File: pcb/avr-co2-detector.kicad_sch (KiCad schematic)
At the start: 16 parts

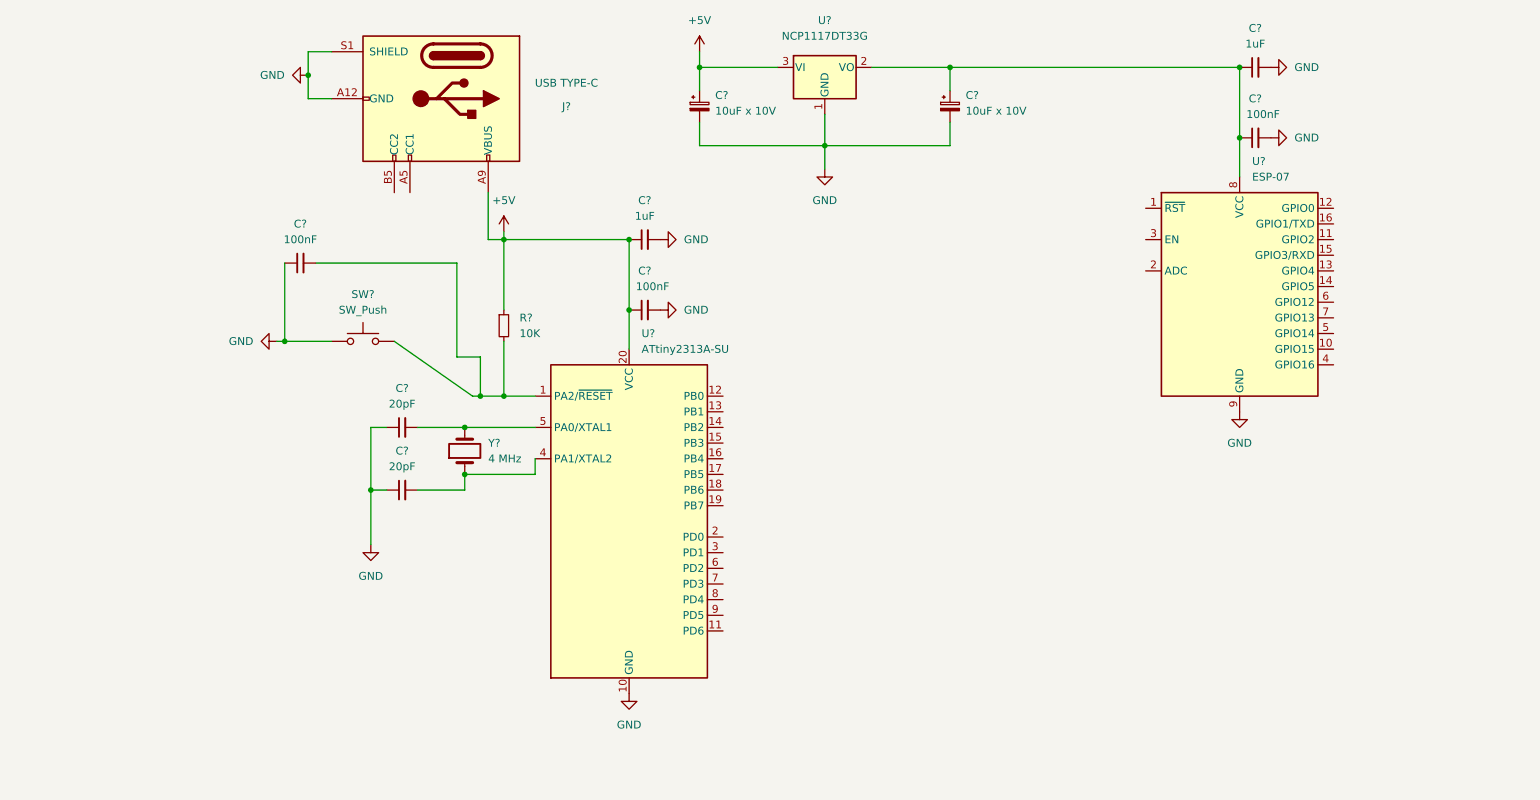
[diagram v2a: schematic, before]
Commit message: Added reset circuit and connector for programming ESP-07
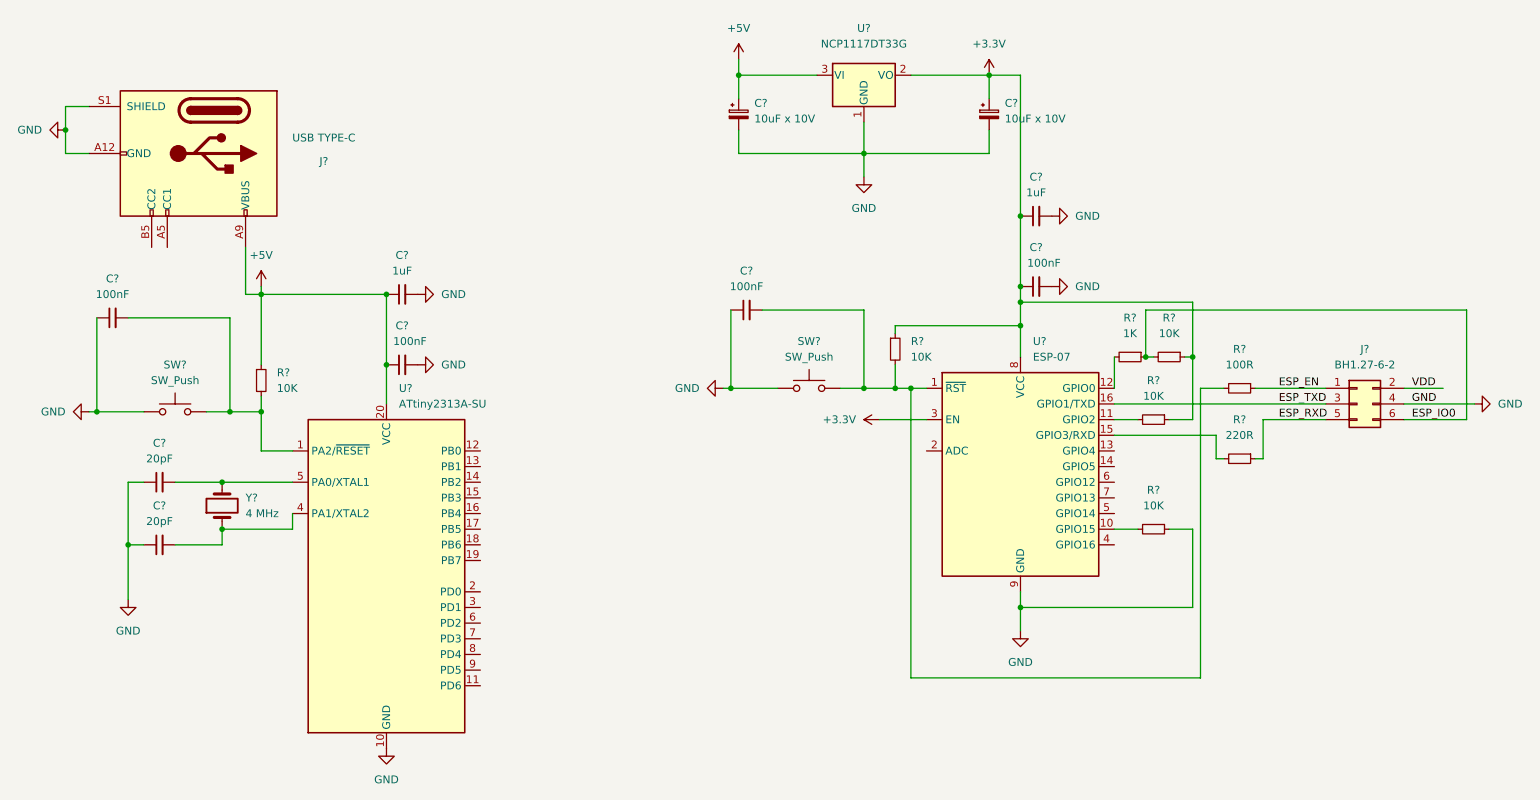
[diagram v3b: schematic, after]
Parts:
- added C?: 100nF, symbol Device:C_Small
- added J?: BH1.27-6-2, symbol Connector_Generic:Conn_02x03_Odd_Even
- added R?: 220R, symbol Device:R_Small
- added R?: 100R, symbol Device:R_Small
- added R? (x4): 10K, symbol Device:R_Small
- added R?: 1K, symbol Device:R_Small
- added SW?: SW_Push, symbol Switch:SW_Push
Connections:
- net GND: now also C?.1, J?.4 (Pin_4), R?.1, SW?.1
- net at U?.1 (~{RST}): now also C?.2, R?.2, R?.2, SW?.2
- net at U?.10 (GPIO15): now also R?.2
- net at U?.11 (GPIO2): now also R?.2
- net at U?.12 (GPIO0): now also R?.2
- net at U?.15 (GPIO3/RXD): now also R?.2
- net ESP_TXD: now reaches U?.16 (GPIO1/TXD)
- net ESP_TXD: now also J?.3 (Pin_3)
- net +3.3V: now reaches U?.3 (EN)
- net +3.3V: now also C?.1, C?.1, C?.1, U?.2 (VO), U?.8 (VCC), R?.1, R?.1, R?.1
- new net ESP_EN: J?.1 (Pin_1), R?.1
- new net ESP_IO0: J?.6 (Pin_6), R?.1, R?.2
- new net ESP_RXD: J?.5 (Pin_5), R?.1
- new net VDD: J?.2 (Pin_2)
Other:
- moved on the sheet: C?, J?, R?, SW?, U?, Y?

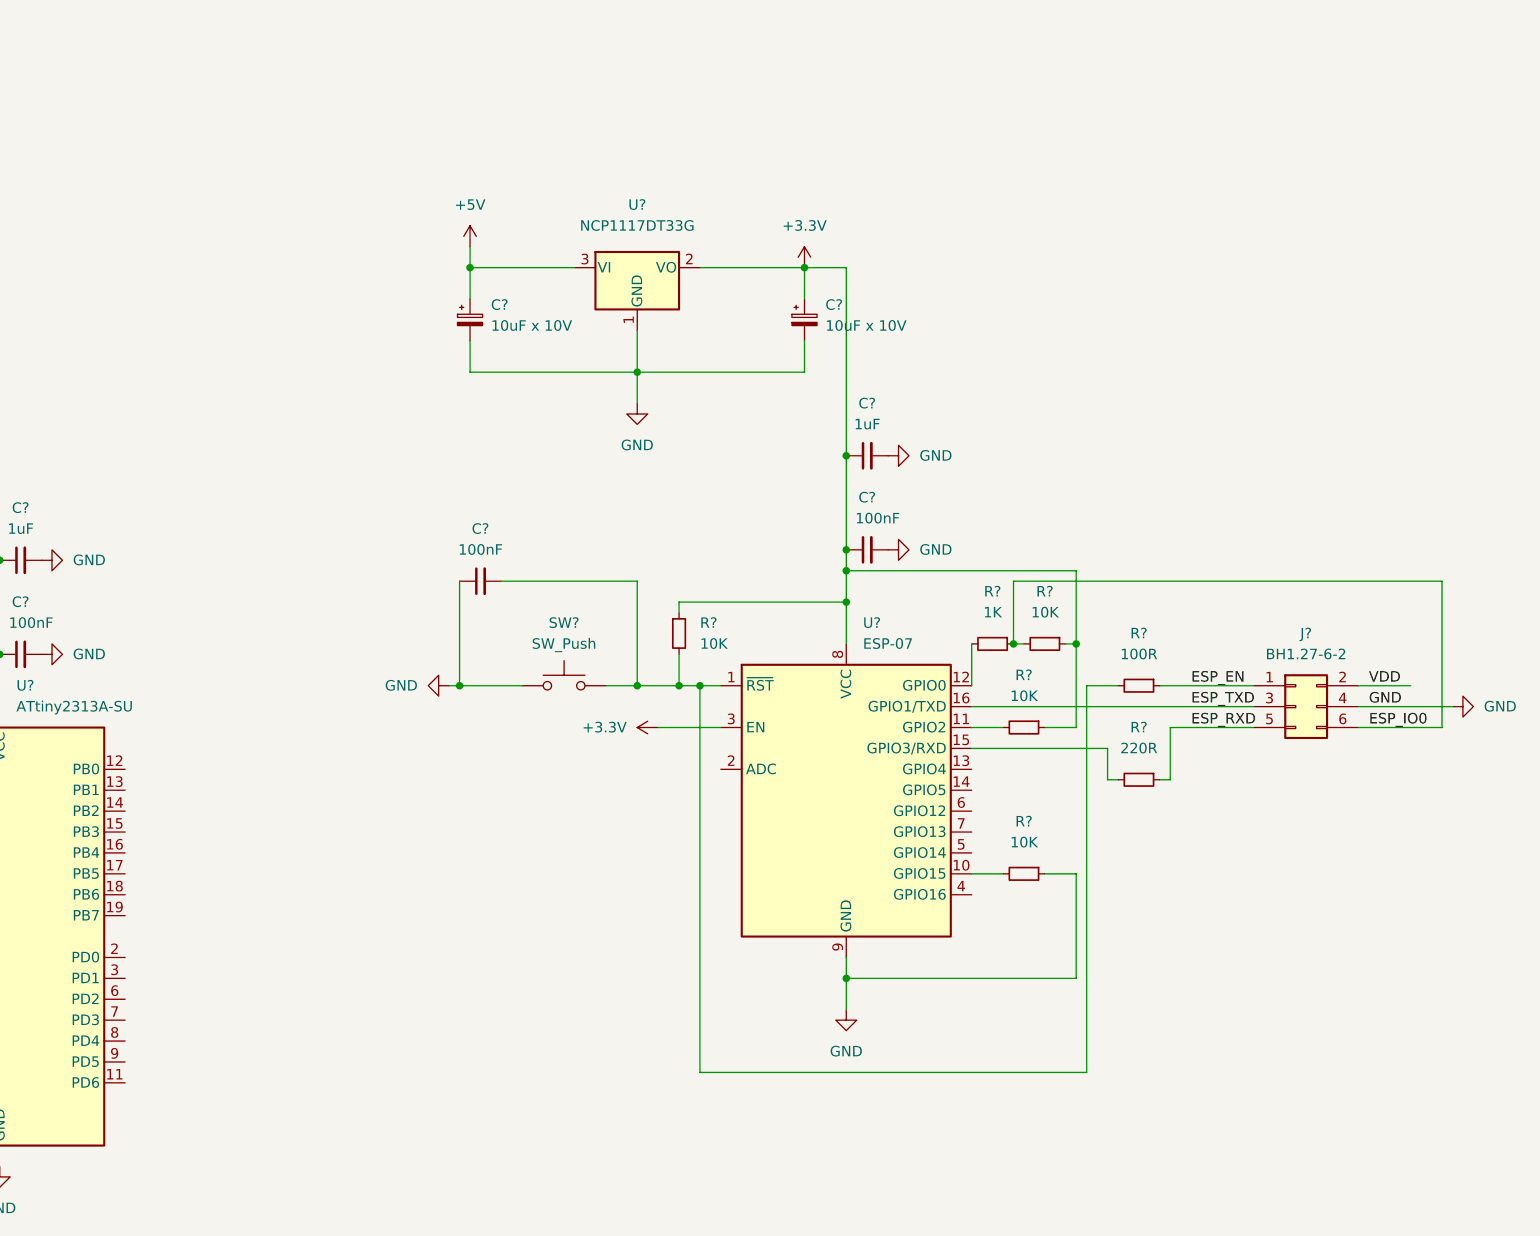
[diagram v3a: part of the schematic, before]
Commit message: Added level shifters for ESP-07 UART
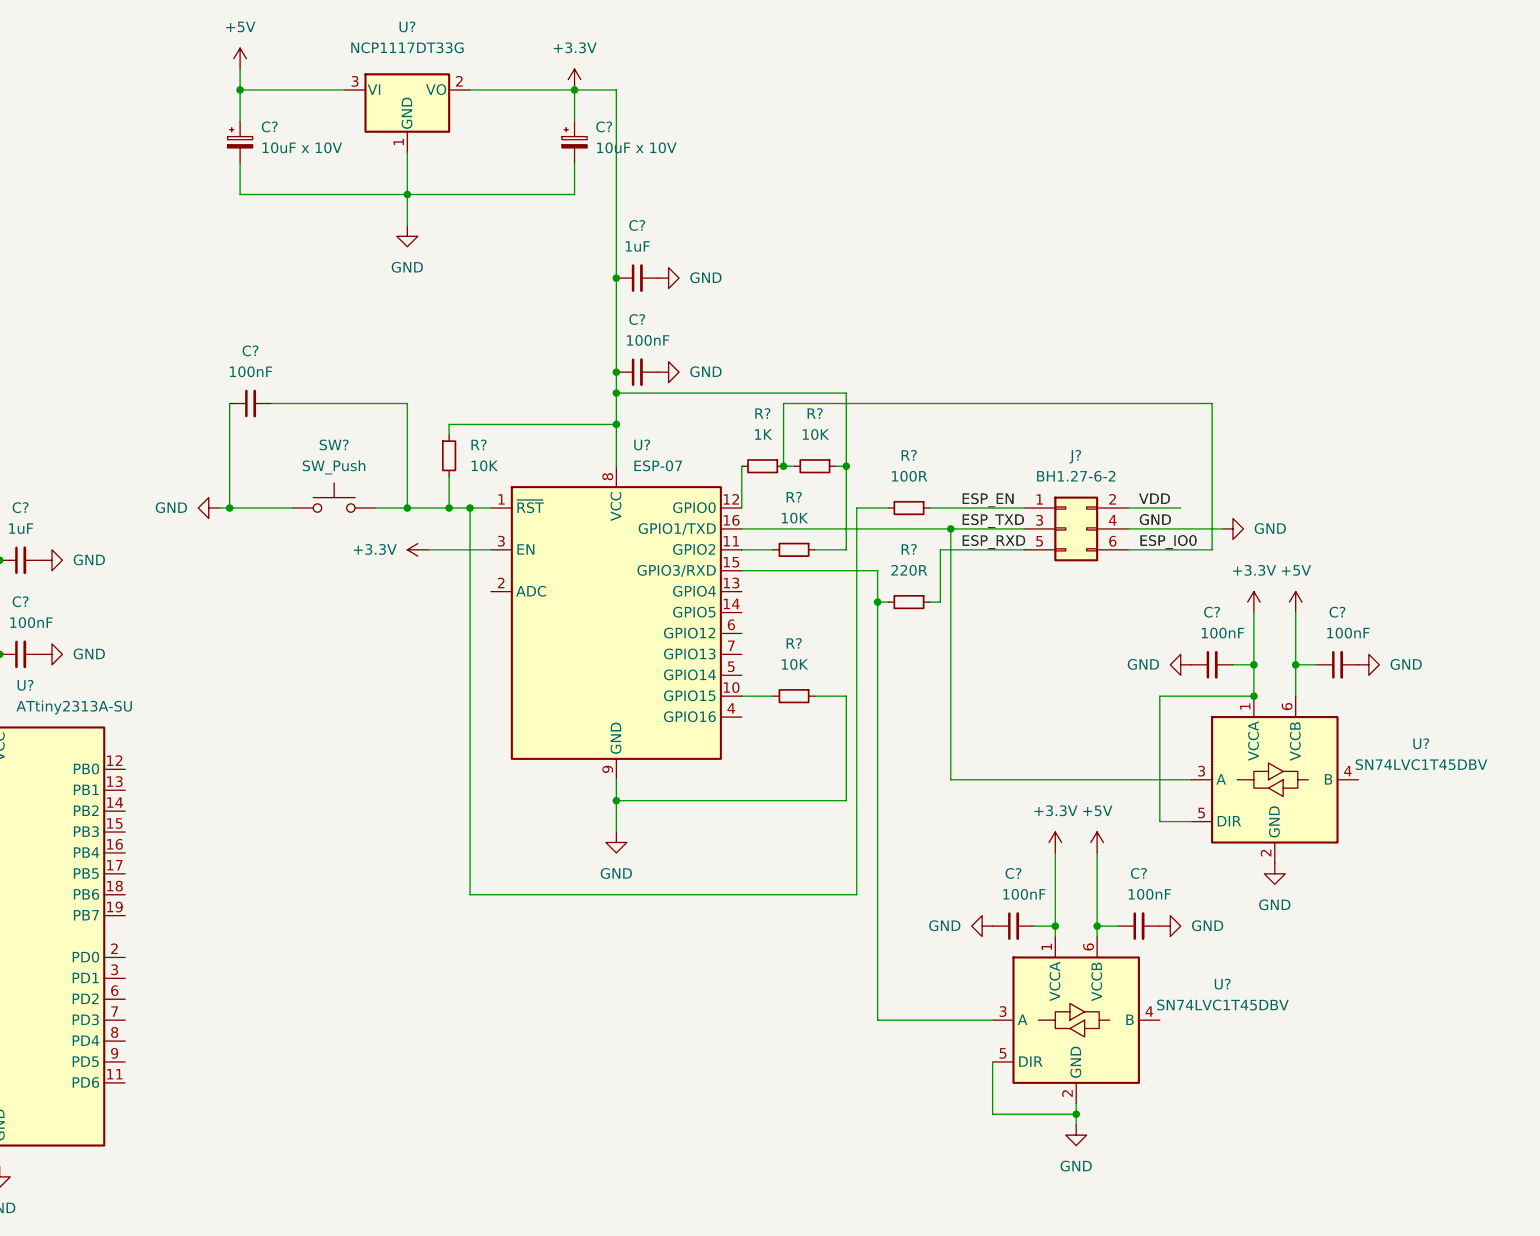
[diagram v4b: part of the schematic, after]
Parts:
- added C? (x4): 100nF, symbol Device:C_Small
- added U? (x2): SN74LVC1T45DBV, Package_TO_SOT_SMD:SOT-23-6, symbol Logic_LevelTranslator:SN74LVC1T45DBV
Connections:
- net +3.3V: now also C?.2, C?.2, U?.1 (VCCA), U?.1 (VCCA), U?.5 (DIR)
- net +5V: now also C?.1, C?.1, U?.6 (VCCB), U?.6 (VCCB)
- net ESP_TXD: now also U?.3 (A)
- net GND: now also C?.1, C?.1, C?.2, C?.2, U?.2 (GND), U?.2 (GND), U?.5 (DIR)
- net at R?.2, U?.15 (GPIO3/RXD): now also U?.3 (A)
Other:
- moved on the sheet: C?, J?, R?, SW?, U?

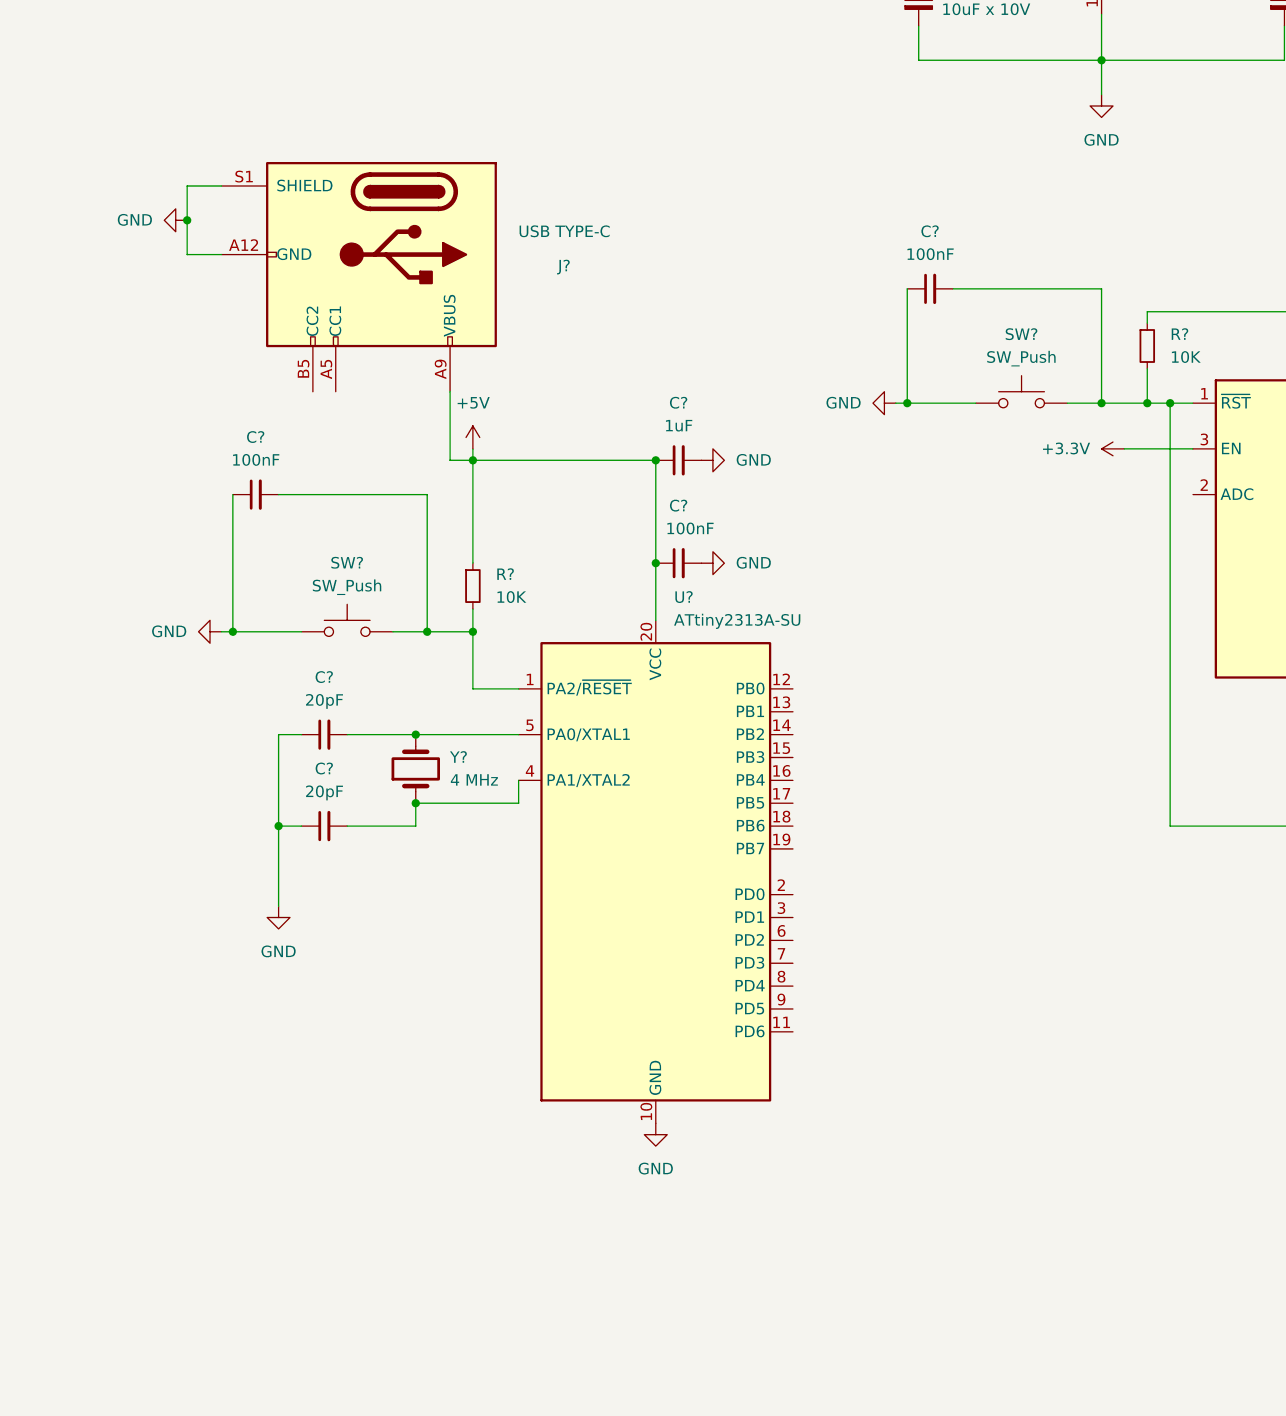
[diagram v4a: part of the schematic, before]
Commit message: Added connector for programming ATtiny2313A
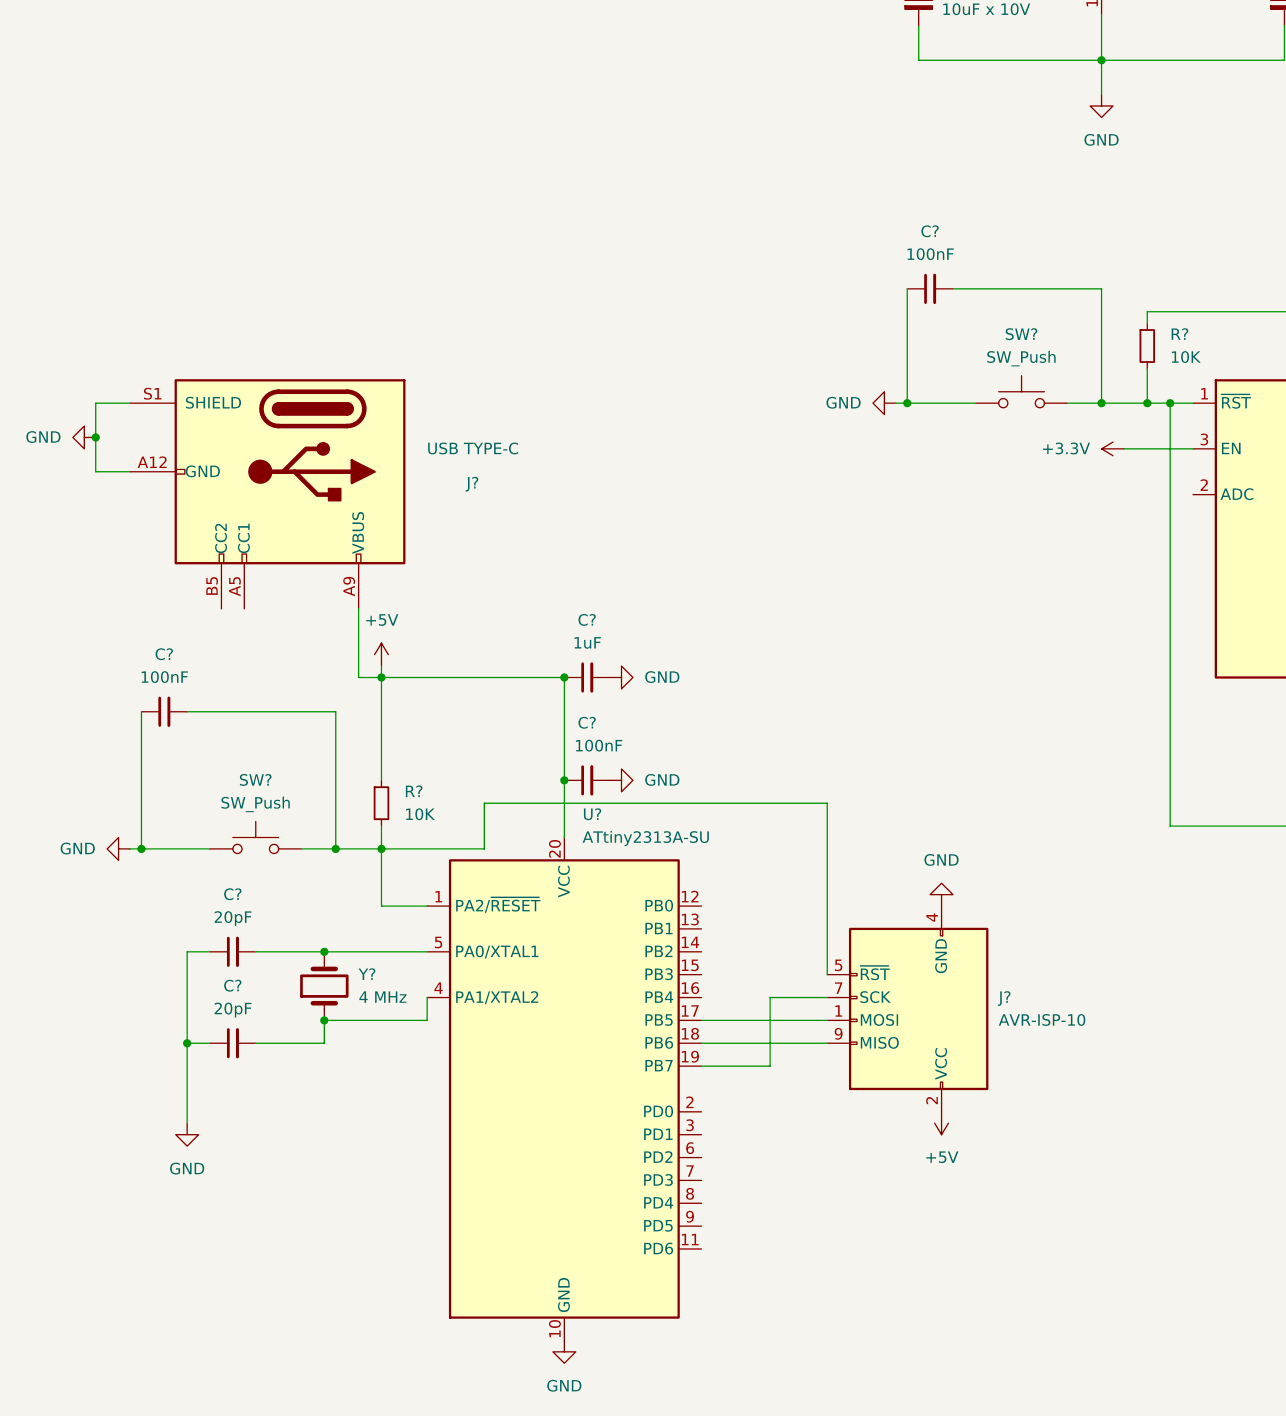
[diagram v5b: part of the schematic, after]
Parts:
- added J?: AVR-ISP-10, symbol Connector:AVR-ISP-10
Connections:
- net +5V: now also J?.2 (VCC)
- net GND: now also J?.10 (GND), J?.4 (GND), J?.6 (GND), J?.8 (GND)
- net at C?.2, R?.2, SW?.2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: now also J?.5 (~{RST})
- net at U?.17 (PB5): now also J?.1 (MOSI)
- net at U?.18 (PB6): now also J?.9 (MISO)
- net at U?.19 (PB7): now also J?.7 (SCK)
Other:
- moved on the sheet: C?, J?, R?, SW?, U?, Y?
